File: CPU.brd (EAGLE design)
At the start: 105.4 x 56.8 mm, 4 parts, among them IC5 HM62256DIP

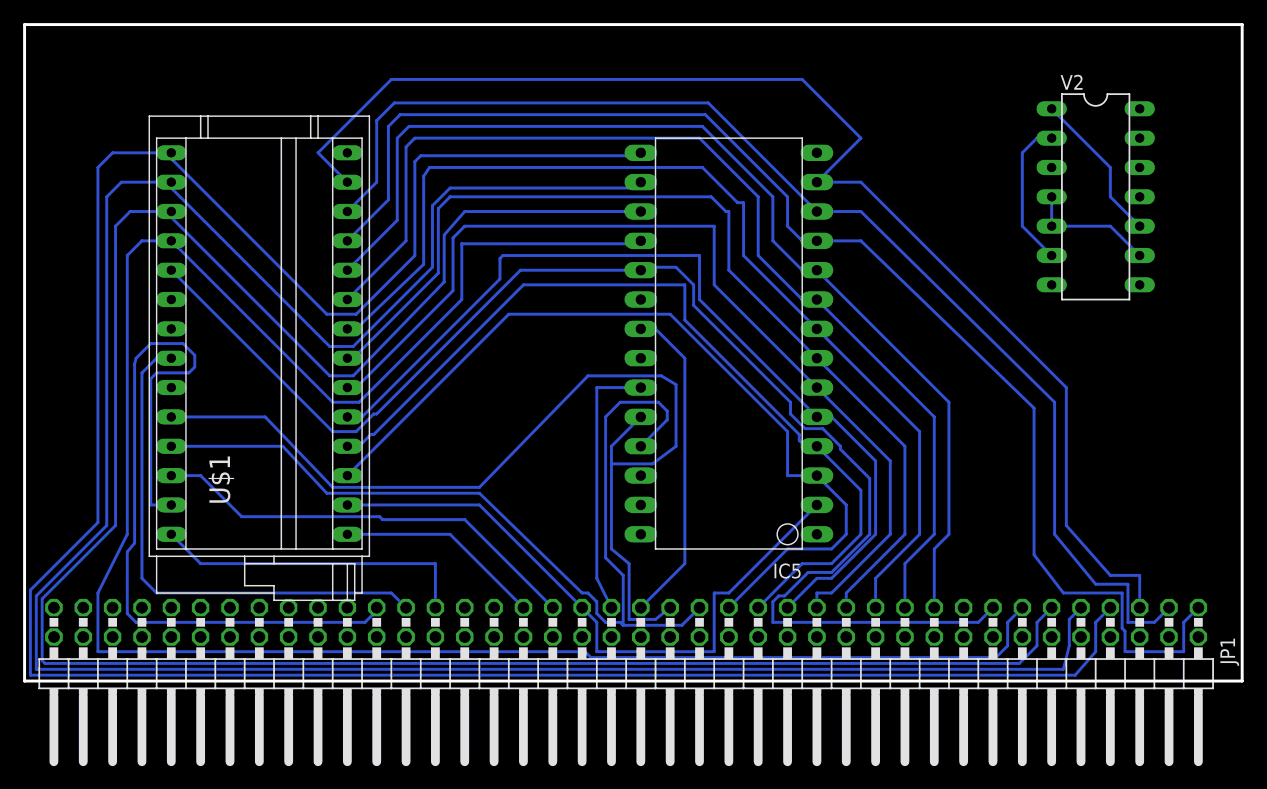
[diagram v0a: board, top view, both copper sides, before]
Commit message: Move away Serial CF
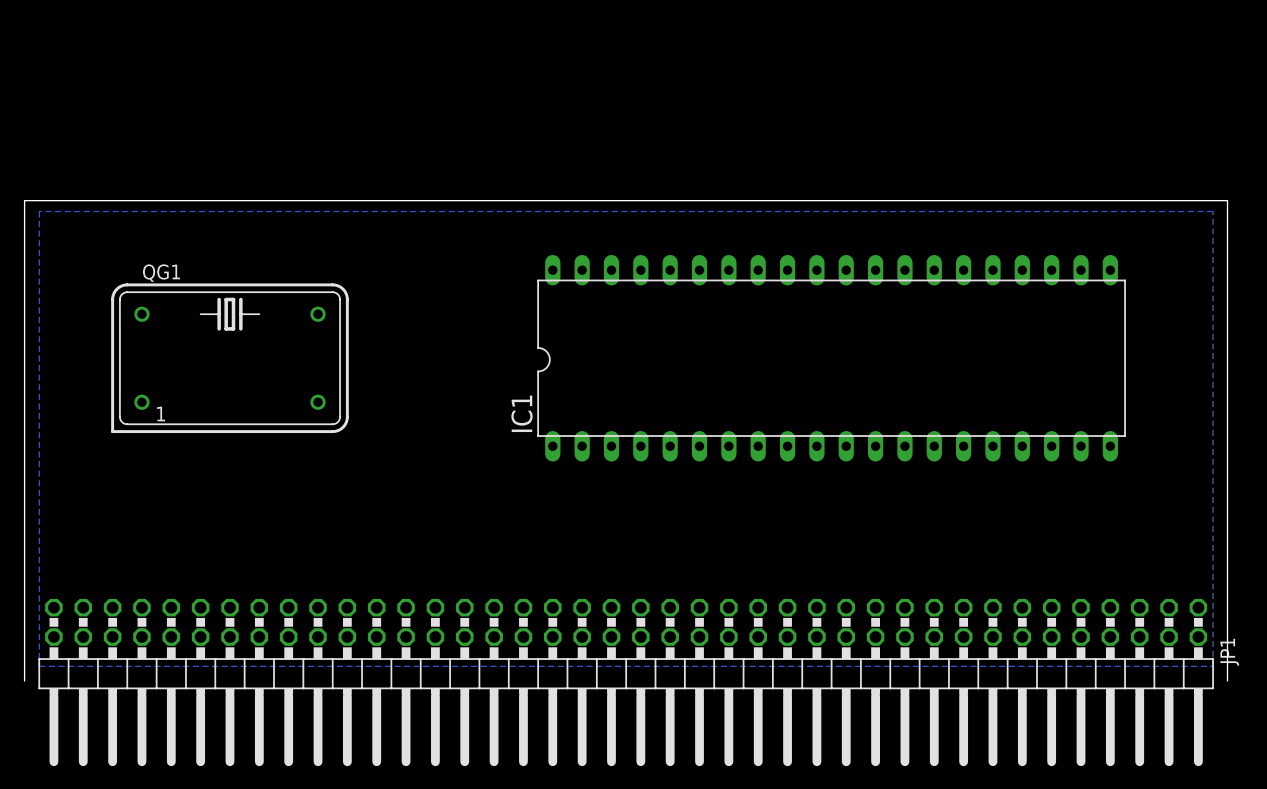
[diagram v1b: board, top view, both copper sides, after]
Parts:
- removed IC5: HM62256DIP, jean:HM62256-DIP
- removed U$1: AT28C256ZIF, bt_memory:DIL28-ZIF
- removed V2: 74HC00N, 74ttl-din:DIL14
- added IC1: Z80CPU, zilog:DIL40
- added QG1: 6 MHz, crystal:DIL14S
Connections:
- removed net !MREQ: JP1.61, V2.1, V2.10
- removed net !RD: IC5.22, JP1.55, U$1.22
- removed net !WR: IC5.27, JP1.57, U$1.27
- removed net N$2: U$1.20, V2.8
- removed net N$4: V2.2, V2.6
- new net !RESET: IC1.26, JP1.79
- new net CLOCK: IC1.6, JP1.63, QG1.8
- new net N$1: IC1.27, JP1.75
- new net N$10: IC1.22, JP1.57
- new net N$14: IC1.21, JP1.55
- new net N$16: IC1.20, JP1.59
- new net N$22: IC1.23, JP1.67
- new net N$8: IC1.19, JP1.61
- new net WAIT: IC1.24, JP1.65
- net A0: now also IC1.30; no longer IC5.10, U$1.10
- net A1: now also IC1.31; no longer IC5.9, U$1.9
- net A10: now also IC1.40; no longer IC5.21, U$1.21
- net A11: now also IC1.1; no longer IC5.23, U$1.23
- net A12: now also IC1.2; no longer IC5.2, U$1.2
- net A13: now also IC1.3; no longer IC5.26, U$1.26
- net A14: now also IC1.4; no longer IC5.1, U$1.1
- net A15: now also IC1.5; no longer V2.4, V2.5, V2.9
- net A2: now also IC1.32; no longer IC5.8, U$1.8
- net A3: now also IC1.33; no longer IC5.7, U$1.7
- net A4: now also IC1.34; no longer IC5.6, U$1.6
- net A5: now also IC1.35; no longer IC5.5, U$1.5
- net A6: now also IC1.36; no longer IC5.4, U$1.4
- net A7: now also IC1.37; no longer IC5.3, U$1.3
- net A8: now also IC1.38; no longer IC5.25, U$1.25
- net A9: now also IC1.39; no longer IC5.24, U$1.24
- net D0: now also IC1.14; no longer IC5.11, U$1.11
- net D1: now also IC1.15; no longer IC5.12, U$1.12
- net D2: now also IC1.12; no longer IC5.13, U$1.13
- net D3: now also IC1.8; no longer IC5.15, U$1.15
- net D4: now also IC1.7; no longer IC5.16, U$1.16
- net D5: now also IC1.9; no longer IC5.17, U$1.17
- net D6: now also IC1.10; no longer IC5.18, U$1.18
- net D7: now also IC1.13; no longer IC5.19, U$1.19
- net GND: now also IC1.29, QG1.7; no longer IC5.14, U$1.14, V2.7
- net N$9: now also IC1.18, JP1.71; no longer IC5.20, V2.3
- net VCC: now also IC1.11, IC1.16, IC1.17, IC1.25, JP1.69, JP1.73, JP1.77, QG1.14; no longer IC5.28, U$1.28, V2.14
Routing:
- net D3: track 208.0 -> 0.00 mm
- net D4: track 200.1 -> 0.00 mm
- net D5: track 191.5 -> 0.00 mm
- net D6: track 177.5 -> 0.00 mm
- net D7: track 118.5 -> 0.00 mm
- net D0: track 116.1 -> 0.00 mm
- net D2: track 112.7 -> 0.00 mm
- net D1: track 106.1 -> 0.00 mm
- net A1: track 91.9 -> 0.00 mm
- net A0: track 91.8 -> 0.00 mm
- net A2: track 88.8 -> 0.00 mm
- net A3: track 85.3 -> 0.00 mm
- net A9: track 85.2 -> 0.00 mm
- net A4: track 82.9 -> 0.00 mm
- net A8: track 82.2 -> 0.00 mm
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- added copper zone on layer 16, net GND
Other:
- board size 105.4 x 56.8 mm -> 104.1 x 41.6 mm
